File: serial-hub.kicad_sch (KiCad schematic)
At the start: 55 parts, among them J1 USB_C_Receptacle_USB2.0, J10 RJ45_LED_Shielded, J2 Conn_01x04_Male, J3 Conn_01x03_Male, J4 Conn_01x03_Male, J5 RJ45_LED_Shielded, J6 RJ45_LED_Shielded, J7 Conn_01x03_Male, J8 Conn_01x03_Male, J9 RJ45_LED_Shielded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

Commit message: schematic: fix incorrect JLC part assignment
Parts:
- R1, R2: LCSC C17606 -> C25905
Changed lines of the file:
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@@
       (effects (font (size 1.27 1.27)) hide)
     )
-    (property "LCSC" "C17606" (id 4) (at 60.96 161.2899 0)
+    (property "LCSC" "C25905" (id 4) (at 60.96 161.2899 0)
       (effects (font (size 1.27 1.27)) hide)
     )
@@
       (effects (font (size 1.27 1.27)) hide)
     )
-    (property "LCSC" "C17606" (id 4) (at 71.12 161.2899 0)
-      (effects (font (size 1.27 1.27)) hide)
-    )
+    (property "LCSC" "C25905" (id 4) (at 71.12 161.2899 0)
+      (effects (font (size 1.27 1.27)) hide)
+    )

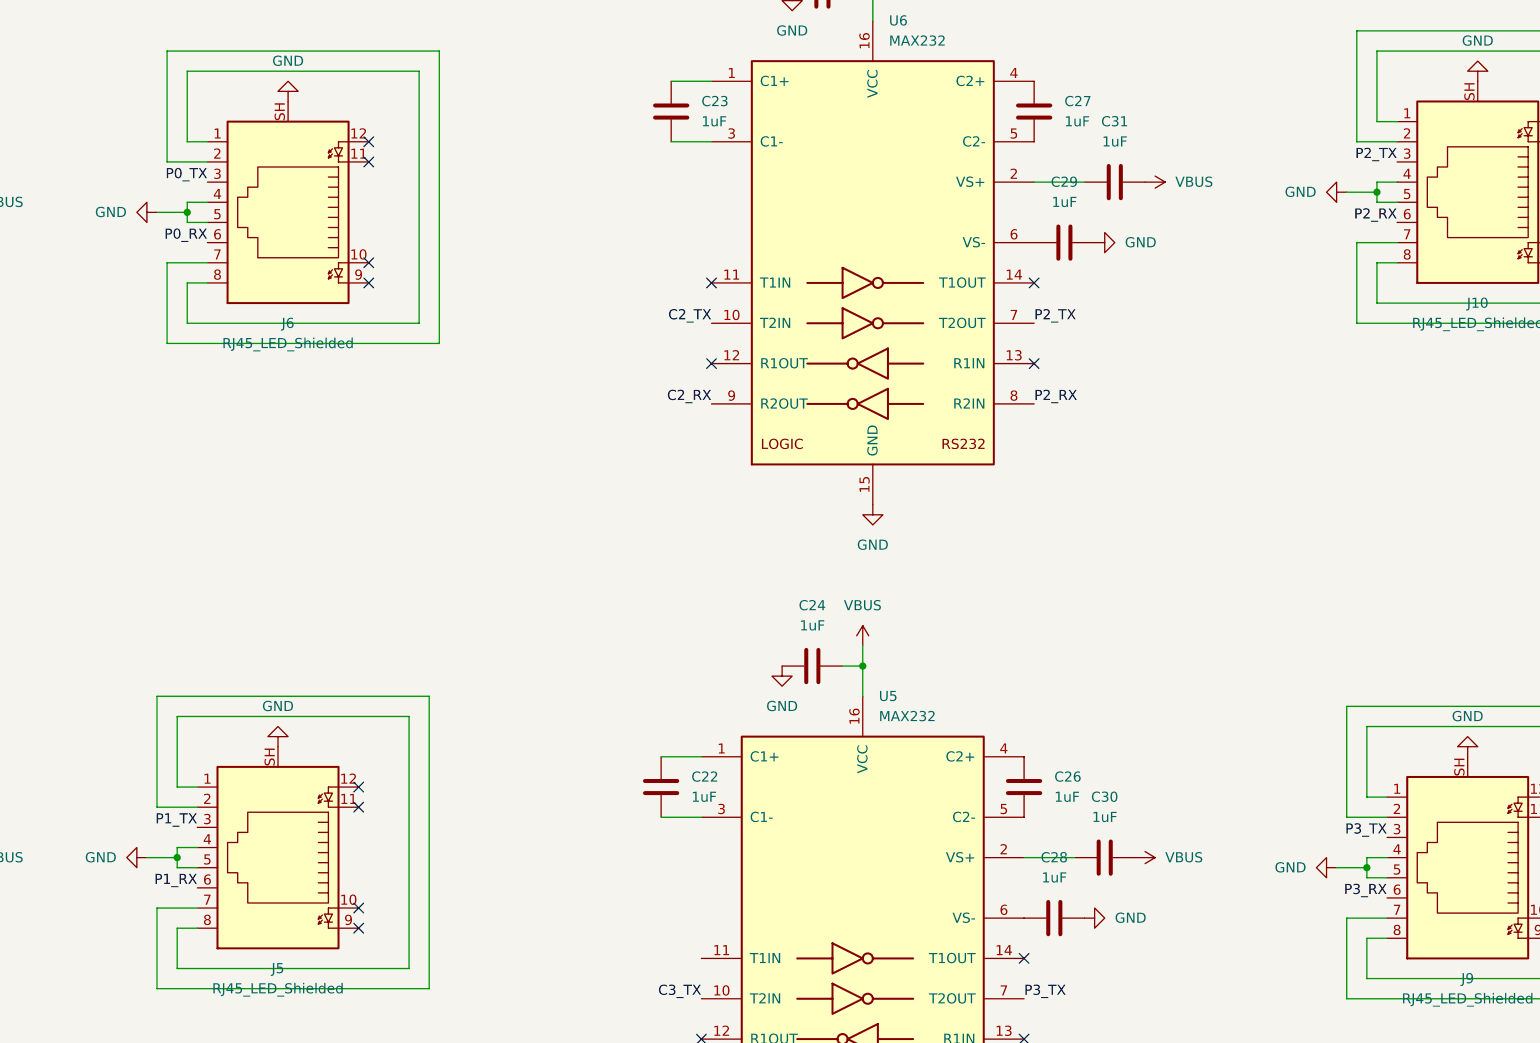
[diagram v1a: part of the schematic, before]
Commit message: board: fix wrong RJ45 pins
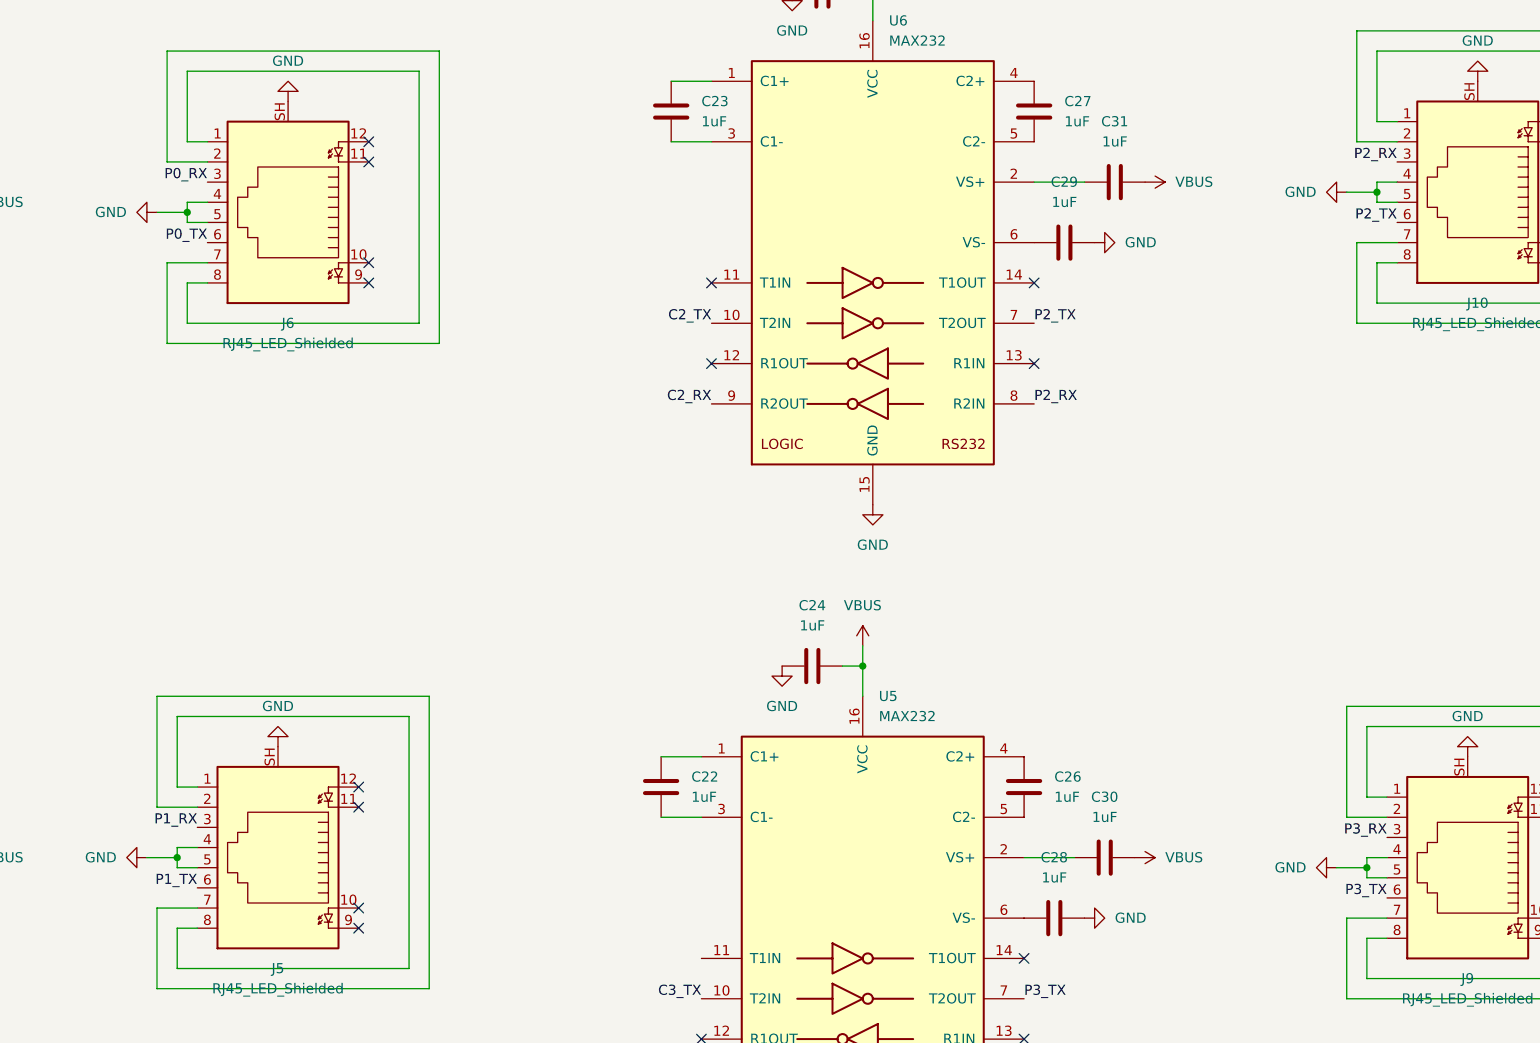
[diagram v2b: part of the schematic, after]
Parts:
- J10, J5, J6, J9: footprint Connector_RJ:RJ45_Hanrun_HR911105A -> Connector_RJ:RJ45_Amphenol_54602-x08_Horizontal; LCSC C12074 -> C2847314
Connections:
- net P0_RX: now also J6.3; no longer J6.6
- net P0_TX: now also J6.6; no longer J6.3
- net P1_RX: now also J5.3; no longer J5.6
- net P1_TX: now also J5.6; no longer J5.3
- net P2_RX: now also J10.3; no longer J10.6
- net P2_TX: now also J10.6; no longer J10.3
- net P3_RX: now also J9.3; no longer J9.6
- net P3_TX: now also J9.6; no longer J9.3
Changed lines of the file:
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@@
     (effects (font (size 1.27 1.27)) (justify right bottom))
   )
-  (label "P3_TX" (at 506.73 133.35 180)
+  (label "P3_TX" (at 506.73 140.97 180)
     (effects (font (size 1.27 1.27)) (justify right bottom))
   )
@@
     (effects (font (size 1.27 1.27)) (justify right bottom))
   )
-  (label "P1_RX" (at 356.87 139.7 180)
+  (label "P1_RX" (at 356.87 132.08 180)
     (effects (font (size 1.27 1.27)) (justify right bottom))
   )
@@
     (effects (font (size 1.27 1.27)) (justify left bottom))
   )
-  (label "P2_TX" (at 508 48.26 180)
+  (label "P2_TX" (at 508 55.88 180)
     (effects (font (size 1.27 1.27)) (justify right bottom))
   )
@@
     (effects (font (size 1.27 1.27)) (justify right bottom))
   )
-  (label "P0_RX" (at 358.14 58.42 180)
+  (label "P0_RX" (at 358.14 50.8 180)
     (effects (font (size 1.27 1.27)) (justify right bottom))
   )
@@
     (effects (font (size 1.27 1.27)) (justify left bottom))
   )
-  (label "P3_RX" (at 506.73 140.97 180)
-    (effects (font (size 1.27 1.27)) (justify right bottom))
-  )
-  (label "P2_RX" (at 508 55.88 180)
+  (label "P3_RX" (at 506.73 133.35 180)
+    (effects (font (size 1.27 1.27)) (justify right bottom))
+  )
+  (label "P2_RX" (at 508 48.26 180)
     (effects (font (size 1.27 1.27)) (justify right bottom))
   )
@@
     (effects (font (size 1.27 1.27)) (justify left bottom))
   )
-  (label "P1_TX" (at 356.87 132.08 180)
+  (label "P1_TX" (at 356.87 139.7 180)
     (effects (font (size 1.27 1.27)) (justify right bottom))
   )
@@
     (effects (font (size 1.27 1.27)) (justify left bottom))
   )
-  (label "P0_TX" (at 358.14 50.8 180)
+  (label "P0_TX" (at 358.14 58.42 180)
     (effects (font (size 1.27 1.27)) (justify right bottom))
   )
@@
     (property "Reference" "J10" (id 0) (at 518.16 66.04 0))
     (property "Value" "RJ45_LED_Shielded" (id 1) (at 518.16 68.58 0))
-    (property "Footprint" "Connector_RJ:RJ45_Hanrun_HR911105A" (id 2) (at 518.16 51.435 90)
+    (property "Footprint" "Connector_RJ:RJ45_Amphenol_54602-x08_Horizontal" (id 2) (at 518.16 51.435 90)
       (effects (font (size 1.27 1.27)) hide)
     )
@@
       (effects (font (size 1.27 1.27)) hide)
     )
-    (property "LCSC" "C12074" (id 4) (at 518.16 66.04 0)
+    (property "LCSC" "C2847314" (id 4) (at 518.16 66.04 0)
       (effects (font (size 1.27 1.27)) hide)
     )
@@
     (property "Reference" "J9" (id 0) (at 516.89 151.13 0))
     (property "Value" "RJ45_LED_Shielded" (id 1) (at 516.89 153.67 0))
-    (property "Footprint" "Connector_RJ:RJ45_Hanrun_HR911105A" (id 2) (at 516.89 136.525 90)
+    (property "Footprint" "Connector_RJ:RJ45_Amphenol_54602-x08_Horizontal" (id 2) (at 516.89 136.525 90)
       (effects (font (size 1.27 1.27)) hide)
     )
@@
       (effects (font (size 1.27 1.27)) hide)
     )
-    (property "LCSC" "C12074" (id 4) (at 516.89 151.13 0)
+    (property "LCSC" "C2847314" (id 4) (at 516.89 151.13 0)
       (effects (font (size 1.27 1.27)) hide)
     )
@@
     (property "Reference" "J5" (id 0) (at 367.03 149.86 0))
     (property "Value" "RJ45_LED_Shielded" (id 1) (at 367.03 152.4 0))
-    (property "Footprint" "Connector_RJ:RJ45_Hanrun_HR911105A" (id 2) (at 367.03 135.255 90)
+    (property "Footprint" "Connector_RJ:RJ45_Amphenol_54602-x08_Horizontal" (id 2) (at 367.03 135.255 90)
       (effects (font (size 1.27 1.27)) hide)
     )
@@
       (effects (font (size 1.27 1.27)) hide)
     )
-    (property "LCSC" "C12074" (id 4) (at 367.03 149.86 0)
+    (property "LCSC" "C2847314" (id 4) (at 367.03 149.86 0)
       (effects (font (size 1.27 1.27)) hide)
     )
@@
     (property "Reference" "J6" (id 0) (at 368.3 68.58 0))
     (property "Value" "RJ45_LED_Shielded" (id 1) (at 368.3 71.12 0))
-    (property "Footprint" "Connector_RJ:RJ45_Hanrun_HR911105A" (id 2) (at 368.3 53.975 90)
+    (property "Footprint" "Connector_RJ:RJ45_Amphenol_54602-x08_Horizontal" (id 2) (at 368.3 53.975 90)
       (effects (font (size 1.27 1.27)) hide)
     )
@@
       (effects (font (size 1.27 1.27)) hide)
     )
-    (property "LCSC" "C12074" (id 4) (at 368.3 68.58 0)
+    (property "LCSC" "C2847314" (id 4) (at 368.3 68.58 0)
       (effects (font (size 1.27 1.27)) hide)
     )
@@
     )
     (path "/6546bd67-b0b5-4d6d-a231-4407a8c0258a"
-      (reference "J5") (unit 1) (value "RJ45_LED_Shielded") (footprint "Connector_RJ:RJ45_Hanrun_HR911105A")
+      (reference "J5") (unit 1) (value "RJ45_LED_Shielded") (footprint "Connector_RJ:RJ45_Amphenol_54602-x08_Horizontal")
     )
     (path "/b55c02bf-687a-43fb-bbd3-8a8003664cbb"
-      (reference "J6") (unit 1) (value "RJ45_LED_Shielded") (footprint "Connector_RJ:RJ45_Hanrun_HR911105A")
+      (reference "J6") (unit 1) (value "RJ45_LED_Shielded") (footprint "Connector_RJ:RJ45_Amphenol_54602-x08_Horizontal")
     )
     (path "/9d05563b-be1e-4225-960b-03e4ded4882d"
@@
     )
     (path "/579ba7af-1b58-42ec-b597-edf795ff7ebe"
-      (reference "J9") (unit 1) (value "RJ45_LED_Shielded") (footprint "Connector_RJ:RJ45_Hanrun_HR911105A")
+      (reference "J9") (unit 1) (value "RJ45_LED_Shielded") (footprint "Connector_RJ:RJ45_Amphenol_54602-x08_Horizontal")
     )
     (path "/4a6ae525-739a-4852-b17c-824d3337c4e5"
-      (reference "J10") (unit 1) (value "RJ45_LED_Shielded") (footprint "Connector_RJ:RJ45_Hanrun_HR911105A")
+      (reference "J10") (unit 1) (value "RJ45_LED_Shielded") (footprint "Connector_RJ:RJ45_Amphenol_54602-x08_Horizontal")
     )
     (path "/61cfd897-704c-4f79-a5b3-b230db74e473"
